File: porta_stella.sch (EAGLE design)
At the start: 80 parts, among them IC1 74LS00D, T1 2N3904, T2 PN3906, T3 PN3906, T4 PN3906, X1 SSW-112-02-G-Q

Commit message: Started work on controller daughterboard
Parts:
- removed C12: 1F, resistor:CPOL-USE3.5-8
- removed C13: 100nF, resistor:C-USC0805
- removed ON/OFF: ON/OFF, special:SW_DIP-1
- removed PAD1: AUD, wirepad:WIREPAD4,16O1,6
- removed PAD2: CVID, wirepad:WIREPAD4,16O1,6
- removed SV1: (no value), con-lstb:MA03-1
- removed USB1: ZX62-B-5PA, Seeed-Connector:MICRO-USB-SMD(ZX62-B-5PA)
- added AUD: AUD, wirepad:WIREPAD2,54/1,1
- added C22: 10uf, adafruit:C-USC0805
- added C5: 10uF, resistor:C-USC1210
- added C6: 2.2uF, adafruit:C-USC0805
- added C7: 0.1uF, adafruit:C-USC0805
- added CHRG/LBO: ORANGE, piboy_new:ADAFRUIT_LEDCHIPLED_0603
- added CN4: MicroUSB, microbuilder:USBMICRO_20329
- added CVID: CVID, wirepad:WIREPAD2,54/1,1
- added DONE: GREEN, piboy_new:ADAFRUIT_LEDCHIPLED_0603
- added GND_A: GND_A, wirepad:WIREPAD2,54/1,1
- added GND_V: GND_V, wirepad:WIREPAD2,54/1,1
- added L1: 6.8uH, microbuilder:INDUCTORTDK_VLC5045
- added LBO: RED, piboy_new:ADAFRUIT_LEDCHIPLED_0603
- added ON: BLUE, piboy_new:ADAFRUIT_LEDCHIPLED_0603
- added ON/OFF1: ON/OFF, special:SW_DIP-1
- added R13, R36, R44, R45: 1K, adafruit:R-US_R0805
- added R37, R39: 200K, adafruit:R-US_R0805
- added R38, R41: 1.87M, adafruit:R-US_R0805
- added R40: 340K, adafruit:R-US_R0805
- added R42: 270K, adafruit:R-US_R0805
- added R43, R47: 100K, adafruit:R-US_R0805
- added R46: 1.0K, adafruit:R-US_R0805
- added SV2: (no value), con-lstb:MA10-1
- added T5: MMUN2133LT1G, piboy_new:TRANSISTOR_MUN2113T1-PNP_DRIVER-SC59-BEC
- added THERM: 15K, adafruit:R-US_R0805
- added U1: TPS61090RSAR, microbuilder:VREG_TPS6103X
- added U2: MCP73871, microbuilder:MCP73871
- C21: value 100nF -> 10uF; device resistor:C-USC0805 -> resistor:C-USC1210
- C9: value 68nF -> 10uF; device resistor:C-USC0805 -> resistor:C-USC1210
- S3, S4: device SparkFun-Switches:MOMENTARY-SWITCH-SPST-PTH-6.0MM-KIT -> SparkFun-Switches:MOMENTARY-SWITCH-SPST-SMD-6.0X3.5MM
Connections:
- new net BOOST_ENABLE: ON/OFF1.1, R37.2, U1.EN
- new net LBO: T5.B, U1.LBO
- new net N$10: L1.2, U1.SW
- new net N$12: R40.2, R41.1, U1.LBI
- new net N$22: LBO.A, R13.1
- new net N$37: R38.1, R39.2, U1.FB
- new net N$41: R13.2, T5.C
- new net N$42: ON.A, R36.2
- new net N$43: R42.1, R43.1, U2.VPCC
- new net N$44: R45.1, U2.STAT2
- new net N$45: R44.1, U2.STAT1/LBO
- new net N$46: R46.2, U2.PROG1
- new net N$47: THERM.2, U2.THERM
- new net N$48: DONE.C, R45.2
- new net N$49: CHRG/LBO.C, R44.2
- new net N$50: R47.2, U2.PROG3
- new net VBAT: C5.1, C7.1, L1.1, R37.1, R41.2, T5.E, U1.VBAT, U2.VOUT1, U2.VOUT2
- new net VLIPO: C21.1, U2.VBAT1, U2.VBAT2, U2.VBATSENS
- net +5V: now also C6.1, C9.1, R36.1, R38.2, SV3.2, U1.VOUT; no longer C12.+, C13.1, ON/OFF.2
- net GND: now also C22.2, C5.2, C6.2, C7.2, CN4.D+, CN4.D-, CN4.GND, CN4.ID, GND_A.P, GND_V.P, LBO.C, ON.C, ON/OFF1.2, R39.1, R40.1, R43.2, R46.1, R47.1, SV2.1, THERM.1, U1.GND, U1.PGND, U1.SYNC, U2.THERMAL, U2.VSS1, U2.VSS2; no longer C12.-, C13.2, SV1.2, SV1.3, USB1.D+, USB1.D-, USB1.GND, USB1.ID, USB1.SHIELD
- net LFT_FIRE: now also SV2.4
- net LFT_JOY_DWN: now also SV2.9
- net LFT_JOY_LFT: now also SV2.8
- net LFT_JOY_RGT: now also SV2.7
- net LFT_JOY_UP: now also SV2.10
- net LFT_PADDLE_A: now also SV2.6
- net LFT_PADDLE_B: now also SV2.5; no longer C9.1
- net N$25: now also CVID.P; no longer PAD2.P
- net N$28: now also AUD.P; no longer PAD1.P
- net P_SW: now also SV2.3
- net VBUS: now also C22.1, CHRG/LBO.A, CN4.VBUS, DONE.A, R42.2, U2./TE, U2.CE, U2.PROG2, U2.SEL, U2.VIN1, U2.VIN2; no longer ON/OFF.1, SV1.1, USB1.VBUS
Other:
- note added: "1.0K = 1000mA"
- note added: "10K NTC Thermistor:"
- note added: "2.0K = 500mA"
- note added: "6.8uH power w/2A current"
- note added: "Charge Rate = 1000V/PROG1"
- note added: "No Thermistor:"
- note added: "RT1 = 0, RT2 = 10K"
- note added: "RT1 = TBD, RT2 = TBD"
- note added: "See Pg 15 1st para"
- moved on the sheet: C21, C9

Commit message: reworked the shape
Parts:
- removed SV2, SV3: (no value), con-lstb:MA10-1
- added J1: PJ-393, Seeed-Connector:AUDIO-JACK-PJ-393(8P-SMD)
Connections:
- net +5V: no longer SV3.2
- net GND: no longer SV2.1, SV3.1
- net LFT_FIRE: no longer SV2.4, SV3.4
- net LFT_JOY_DWN: no longer SV2.9, SV3.9
- net LFT_JOY_LFT: no longer SV2.8, SV3.8
- net LFT_JOY_RGT: no longer SV2.7, SV3.7
- net LFT_JOY_UP: no longer SV2.10, SV3.10
- net LFT_PADDLE_A: no longer SV2.6, SV3.6
- net LFT_PADDLE_B: no longer SV2.5, SV3.5
- net P_SW: no longer SV2.3, SV3.3
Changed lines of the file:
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@@
 <part name="AUD" library="wirepad" library_urn="urn:adsk.eagle:library:412" deviceset="WIREPAD" device="2,54/1,1" package3d_urn="urn:adsk.eagle:package:30836/1" value="AUD"/>
 <part name="CVID" library="wirepad" library_urn="urn:adsk.eagle:library:412" deviceset="WIREPAD" device="2,54/1,1" package3d_urn="urn:adsk.eagle:package:30836/1" value="CVID"/>
-<part name="GND2" library="supply1" library_urn="urn:adsk.eagle:library:371" deviceset="GND" device=""/>
-<part name="SV3" library="con-lstb" library_urn="urn:adsk.eagle:library:162" deviceset="MA10-1" device="" package3d_urn="urn:adsk.eagle:package:8346/1"/>
 <part name="GND3" library="supply1" library_urn="urn:adsk.eagle:library:371" deviceset="GND" device=""/>
 <part name="R35" library="pot" library_urn="urn:adsk.eagle:library:331" deviceset="EVU" device="A" package3d_urn="urn:adsk.eagle:package:22730/1" technology="F2"/>
-<part name="SV2" library="con-lstb" library_urn="urn:adsk.eagle:library:162" deviceset="MA10-1" device="" package3d_urn="urn:adsk.eagle:package:8346/1"/>
 <part name="GND5" library="supply1" library_urn="urn:adsk.eagle:library:371" deviceset="GND" device=""/>
 <part name="GND_A" library="wirepad" library_urn="urn:adsk.eagle:library:412" deviceset="WIREPAD" device="2,54/1,1" package3d_urn="urn:adsk.eagle:package:30836/1" value="GND_A"/>
 <part name="GND_V" library="wirepad" library_urn="urn:adsk.eagle:library:412" deviceset="WIREPAD" device="2,54/1,1" package3d_urn="urn:adsk.eagle:package:30836/1" value="GND_V"/>
 <part name="GND7" library="supply1" library_urn="urn:adsk.eagle:library:371" deviceset="GND" device=""/>
-<part name="P+16" library="supply1" library_urn="urn:adsk.eagle:library:371" deviceset="+5V" device=""/>
 <part name="U1" library="microbuilder" deviceset="VREG_TPS6103X" device="" value="TPS61090RSAR"/>
 <part name="L1" library="microbuilder" deviceset="INDUCTOR" device="TDK_VLC5045" value="6.8uH"/>
@@
 <part name="GND45" library="supply1" deviceset="GND" device=""/>
 <part name="ON/OFF1" library="special" library_urn="urn:adsk.eagle:library:367" deviceset="SW_DIP-1" device="" package3d_urn="urn:adsk.eagle:package:26661/1" value="ON/OFF"/>
+<part name="J1" library="Seeed-Connector" library_urn="urn:adsk.eagle:library:478" deviceset="AUDIO-JACK-PJ-393(8P-SMD)" device="" package3d_urn="urn:adsk.eagle:package:33126/1" value="PJ-393"/>
 </parts>
 <sheets>
@@
 <instance part="AUD" gate="G$1" x="208.28" y="7.62" rot="R90"/>
 <instance part="CVID" gate="G$1" x="312.42" y="60.96" rot="R180"/>
-<instance part="GND2" gate="1" x="297.18" y="116.84" rot="MR0"/>
-<instance part="SV3" gate="1" x="284.48" y="132.08"/>
 <instance part="GND3" gate="1" x="347.98" y="86.36" rot="MR0"/>
 <instance part="R35" gate="G$1" x="345.44" y="99.06" rot="R270"/>
-<instance part="SV2" gate="1" x="276.86" y="132.08" rot="MR0"/>
 <instance part="GND5" gate="1" x="264.16" y="116.84" rot="MR0"/>
 <instance part="GND_A" gate="G$1" x="330.2" y="55.88" rot="R180"/>
 <instance part="GND_V" gate="G$1" x="342.9" y="55.88" rot="R180"/>
 <instance part="GND7" gate="1" x="320.04" y="43.18" rot="MR0"/>
-<instance part="P+16" gate="1" x="299.72" y="124.46" rot="MR90"/>
 <instance part="U1" gate="G$1" x="-226.06" y="68.58"/>
 <instance part="L1" gate="G$1" x="-254" y="78.74"/>
@@
 <instance part="GND45" gate="1" x="-152.4" y="-50.8"/>
 <instance part="ON/OFF1" gate="G$1" x="-154.94" y="73.66" rot="MR0"/>
+<instance part="J1" gate="G$1" x="312.42" y="17.78"/>
 </instances>
 <busses>
@@
 </segment>
 <segment>
-<pinref part="SV3" gate="1" pin="2"/>
-<wire x1="292.1" y1="124.46" x2="297.18" y2="124.46" width="0.1524" layer="91"/>
-<pinref part="P+16" gate="1" pin="+5V"/>
-</segment>
-<segment>
 <pinref part="R36" gate="G$1" pin="1"/>
 <pinref part="U1" gate="G$1" pin="VOUT"/>
@@
 </segment>
 <segment>
-<wire x1="292.1" y1="121.92" x2="297.18" y2="121.92" width="0.1524" layer="91"/>
-<pinref part="GND2" gate="1" pin="GND"/>
-<wire x1="297.18" y1="121.92" x2="297.18" y2="119.38" width="0.1524" layer="91"/>
-<pinref part="SV3" gate="1" pin="1"/>
-</segment>
-<segment>
 <wire x1="347.98" y1="91.44" x2="347.98" y2="88.9" width="0.1524" layer="91"/>
 <pinref part="GND3" gate="1" pin="GND"/>
@@
 <wire x1="347.98" y1="91.44" x2="345.44" y2="91.44" width="0.1524" layer="91"/>
 <wire x1="345.44" y1="91.44" x2="345.44" y2="93.98" width="0.1524" layer="91"/>
-</segment>
-<segment>
-<pinref part="SV2" gate="1" pin="1"/>
-<wire x1="269.24" y1="121.92" x2="264.16" y2="121.92" width="0.1524" layer="91"/>
-<wire x1="264.16" y1="121.92" x2="264.16" y2="119.38" width="0.1524" layer="91"/>
-<pinref part="GND5" gate="1" pin="GND"/>
 </segment>
 <segment>
@@
 <wire x1="292.1" y1="134.62" x2="297.18" y2="134.62" width="0.1524" layer="91"/>
 <label x="297.18" y="134.62" size="1.778" layer="95"/>
-<pinref part="SV3" gate="1" pin="6"/>
 </segment>
 <segment>
@@
 <wire x1="340.36" y1="96.52" x2="340.36" y2="99.06" width="0.1524" layer="91"/>
 </segment>
-<segment>
-<pinref part="SV2" gate="1" pin="6"/>
-<wire x1="269.24" y1="134.62" x2="264.16" y2="134.62" width="0.1524" layer="91"/>
-<label x="264.16" y="134.62" size="1.778" layer="95" rot="R180"/>
-</segment>
 </net>
 <net name="LFT_PADDLE_B" class="0">
@@
 <wire x1="292.1" y1="132.08" x2="297.18" y2="132.08" width="0.1524" layer="91"/>
 <label x="297.18" y="132.08" size="1.778" layer="95"/>
-<pinref part="SV3" gate="1" pin="5"/>
-</segment>
-<segment>
-<pinref part="SV2" gate="1" pin="5"/>
-<wire x1="269.24" y1="132.08" x2="264.16" y2="132.08" width="0.1524" layer="91"/>
-<label x="264.16" y="132.08" size="1.778" layer="95" rot="R180"/>
 </segment>
 </net>
@@
 <wire x1="292.1" y1="137.16" x2="297.18" y2="137.16" width="0.1524" layer="91"/>
 <label x="297.18" y="137.16" size="1.778" layer="95"/>
-<pinref part="SV3" gate="1" pin="7"/>
-</segment>
-<segment>
-<pinref part="SV2" gate="1" pin="7"/>
-<wire x1="269.24" y1="137.16" x2="264.16" y2="137.16" width="0.1524" layer="91"/>
-<label x="264.16" y="137.16" size="1.778" layer="95" rot="R180"/>
 </segment>
 </net>
@@
 <wire x1="292.1" y1="139.7" x2="297.18" y2="139.7" width="0.1524" layer="91"/>
 <label x="297.18" y="139.7" size="1.778" layer="95"/>
-<pinref part="SV3" gate="1" pin="8"/>
-</segment>
-<segment>
-<pinref part="SV2" gate="1" pin="8"/>
-<wire x1="269.24" y1="139.7" x2="264.16" y2="139.7" width="0.1524" layer="91"/>
-<label x="264.16" y="139.7" size="1.778" layer="95" rot="R180"/>
 </segment>
 </net>
@@
 <wire x1="292.1" y1="142.24" x2="297.18" y2="142.24" width="0.1524" layer="91"/>
 <label x="297.18" y="142.24" size="1.778" layer="95"/>
-<pinref part="SV3" gate="1" pin="9"/>
-</segment>
-<segment>
-<pinref part="SV2" gate="1" pin="9"/>
-<wire x1="269.24" y1="142.24" x2="264.16" y2="142.24" width="0.1524" layer="91"/>
-<label x="264.16" y="142.24" size="1.778" layer="95" rot="R180"/>
 </segment>
 </net>
@@
 <wire x1="292.1" y1="144.78" x2="297.18" y2="144.78" width="0.1524" layer="91"/>
 <label x="297.18" y="144.78" size="1.778" layer="95"/>
-<pinref part="SV3" gate="1" pin="10"/>
-</segment>
-<segment>
-<pinref part="SV2" gate="1" pin="10"/>
-<wire x1="269.24" y1="144.78" x2="264.16" y2="144.78" width="0.1524" layer="91"/>
-<label x="264.16" y="144.78" size="1.778" layer="95" rot="R180"/>
 </segment>
 </net>
@@
 </segment>
 <segment>
-<pinref part="SV3" gate="1" pin="3"/>
 <wire x1="292.1" y1="127" x2="297.18" y2="127" width="0.1524" layer="91"/>
 <label x="297.18" y="127" size="1.778" layer="95"/>
 </segment>
-<segment>
-<pinref part="SV2" gate="1" pin="3"/>
-<wire x1="269.24" y1="127" x2="264.16" y2="127" width="0.1524" layer="91"/>
-<label x="264.16" y="127" size="1.778" layer="95" rot="R180"/>
-</segment>
 </net>
 <net name="LFT_FIRE" class="0">
@@
 <wire x1="292.1" y1="129.54" x2="297.18" y2="129.54" width="0.1524" layer="91"/>
 <label x="297.18" y="129.54" size="1.778" layer="95"/>
-<pinref part="SV3" gate="1" pin="4"/>
 </segment>
 <segment>
@@
 <label x="195.58" y="99.06" size="1.778" layer="95"/>
 </segment>
-<segment>
-<pinref part="SV2" gate="1" pin="4"/>
-<wire x1="269.24" y1="129.54" x2="264.16" y2="129.54" width="0.1524" layer="91"/>
-<label x="264.16" y="129.54" size="1.778" layer="95" rot="R180"/>
-</segment>
-</net>
+</net>

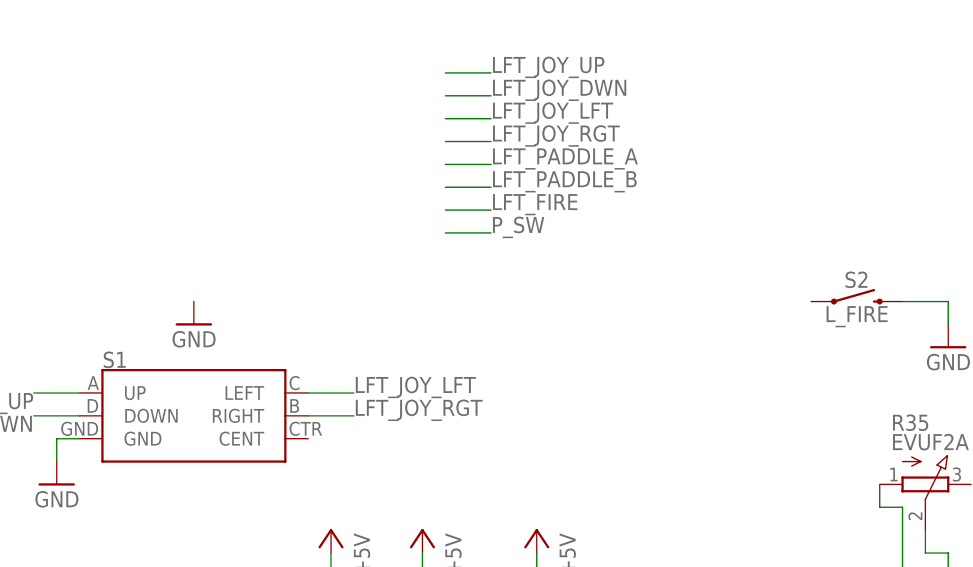
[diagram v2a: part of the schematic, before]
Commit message: included measurements of the screen
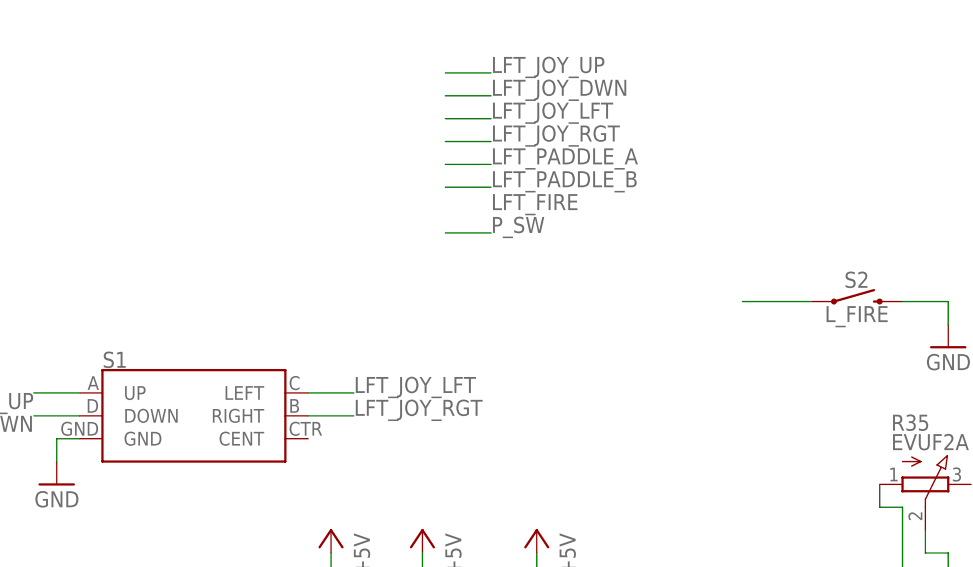
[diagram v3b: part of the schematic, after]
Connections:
- net LFT_FIRE: now also S2.1
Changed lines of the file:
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@@
 <part name="GND3" library="supply1" library_urn="urn:adsk.eagle:library:371" deviceset="GND" device=""/>
 <part name="R35" library="pot" library_urn="urn:adsk.eagle:library:331" deviceset="EVU" device="A" package3d_urn="urn:adsk.eagle:package:22730/1" technology="F2"/>
-<part name="GND5" library="supply1" library_urn="urn:adsk.eagle:library:371" deviceset="GND" device=""/>
 <part name="GND_A" library="wirepad" library_urn="urn:adsk.eagle:library:412" deviceset="WIREPAD" device="2,54/1,1" package3d_urn="urn:adsk.eagle:package:30836/1" value="GND_A"/>
 <part name="GND_V" library="wirepad" library_urn="urn:adsk.eagle:library:412" deviceset="WIREPAD" device="2,54/1,1" package3d_urn="urn:adsk.eagle:package:30836/1" value="GND_V"/>
@@
 <instance part="GND3" gate="1" x="347.98" y="86.36" rot="MR0"/>
 <instance part="R35" gate="G$1" x="345.44" y="99.06" rot="R270"/>
-<instance part="GND5" gate="1" x="264.16" y="116.84" rot="MR0"/>
 <instance part="GND_A" gate="G$1" x="330.2" y="55.88" rot="R180"/>
 <instance part="GND_V" gate="G$1" x="342.9" y="55.88" rot="R180"/>
@@
 <net name="LFT_FIRE" class="0">
 <segment>
-<wire x1="292.1" y1="129.54" x2="297.18" y2="129.54" width="0.1524" layer="91"/>
 <label x="297.18" y="129.54" size="1.778" layer="95"/>
-</segment>
-<segment>
+<pinref part="S2" gate="G$1" pin="1"/>
+<wire x1="325.12" y1="119.38" x2="332.74" y2="119.38" width="0.1524" layer="91"/>
+</segment>
+<segment>
